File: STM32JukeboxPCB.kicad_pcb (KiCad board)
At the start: 4 copper layers, 50 x 70 mm, 104 parts, among them J1 MSD-1-A, J2 Screw_Terminal_1x2, J3 USB_C_Receptacle_USB2.0_16P, J4 AudioJack3_SwitchTR, J5 Conn_01x08_Socket, J6 Conn_01x05, J7 Conn_01x04, J8 Conn_01x04_Pin, J9 Conn_01x02_Pin, SW1 SW_Push, SW2 SW_Push, U1 STM32F411CEUx, U2 PCM5102A, U3 MAX98357A, U4 TLV70233_SOT23-5, U5 HT97226, Y1 Crystal_GND23, Y2 Crystal

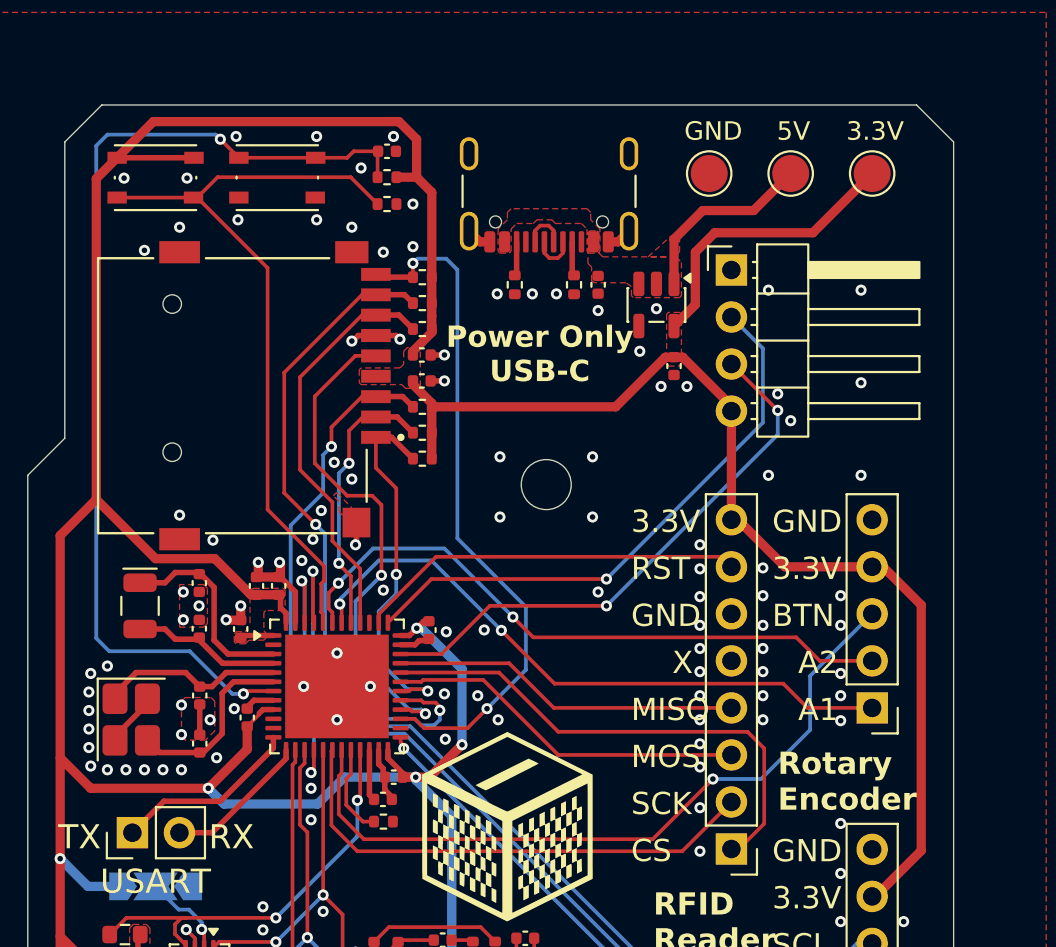
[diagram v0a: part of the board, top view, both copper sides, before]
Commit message: new pcb. added power switch and disc detect button
rfid reading has been unreliable, so added a button that gets pressed when a disc is inserted to lock the current disc that's playing. eliminates the chance of a music disc that's inserted to randomly stop playing due to the rfid reader's wonky detection not catching its presence
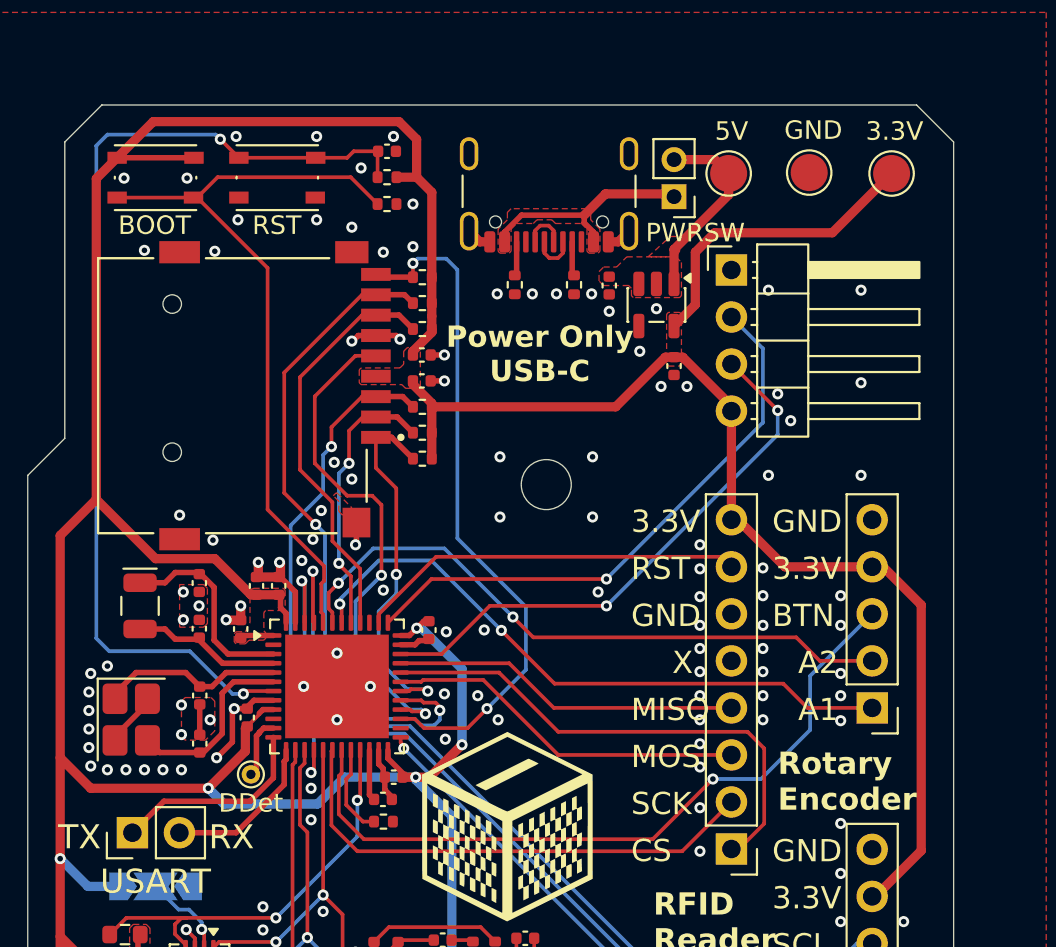
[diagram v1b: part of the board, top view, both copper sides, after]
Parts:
- added DDet: Conn_1x1, TestPoint:TestPoint_THTPad_D1.0mm_Drill0.5mm, F.Cu at (112.0, 86.2)
- added PWRSW: SW_SPST, Connector_PinHeader_2.00mm:PinHeader_1x02_P2.00mm_Vertical, F.Cu at (134.9, 55.0)
- moved TP3 5.40 mm to (142.2, 53.6)
- moved TP1 3.35 mm to (137.8, 53.7)
- moved TP2 1.05 mm to (146.7, 53.7)
- moved C42 0.60 mm to (131.4, 59.8)
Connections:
- J3 pad A4: +5V -> /STM32F411 Sheet/USB_5V
- J3 pad A9: +5V -> /STM32F411 Sheet/USB_5V
- J3 pad B4: +5V -> /STM32F411 Sheet/USB_5V
- J3 pad B9: +5V -> /STM32F411 Sheet/USB_5V
- U1 pad 11: unconnected-(U1-PA1-Pad11) -> /STM32F411 Sheet/Insert_Disc_Detect
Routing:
- net /STM32F411 Sheet/USB_5V: track 0.00 -> 12.2 mm
- net GND: track 53.7 -> 57.5 mm, vias 169 -> 170
- net /STM32F411 Sheet/Insert_Disc_Detect: track 0.00 -> 3.31 mm
- net +3.3V: track 312.2 -> 313.3 mm
- net /STM32F411 Sheet/USART2_TX: track 10.1 -> 11.0 mm
- net /STM32F411 Sheet/USART2_RX: track 7.88 -> 8.64 mm
- added copper zone on F.Cu, net /STM32F411 Sheet/USB_5V
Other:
- board text added: "BOOT"
- board text added: "STM32 RFID Minecraft Jukebox Rev 1.1 10/05/26 Johnathan Guzman"
- board text removed: "STM32 RFID Minecraft Jukebox Rev 1.0 09/11/26 Johnathan Guzman"
